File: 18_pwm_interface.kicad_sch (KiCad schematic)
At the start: 49 parts

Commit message: update -- i don't remeber what
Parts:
- R1, R10, R11, R12, R13, R14, R15, R16, R17, R18, R19, R2, R20, R21, R3, R4, R5, R6, R7, R8, R9: footprint (none) -> Resistor_SMD:R_0805_2012Metric
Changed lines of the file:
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@@
 			)
 		)
-		(property "Footprint" ""
+		(property "Footprint" "Resistor_SMD:R_0805_2012Metric"
 			(at 80.772 97.79 90)
 			(effects
@@
 			)
 		)
-		(property "Footprint" ""
+		(property "Footprint" "Resistor_SMD:R_0805_2012Metric"
 			(at 43.942 48.26 90)
 			(effects
@@
 			)
 		)
-		(property "Footprint" ""
+		(property "Footprint" "Resistor_SMD:R_0805_2012Metric"
 			(at 219.202 97.79 90)
 			(effects
@@
 			)
 		)
-		(property "Footprint" ""
+		(property "Footprint" "Resistor_SMD:R_0805_2012Metric"
 			(at 234.442 49.53 90)
 			(effects
@@
 			)
 		)
-		(property "Footprint" ""
+		(property "Footprint" "Resistor_SMD:R_0805_2012Metric"
 			(at 200.152 48.26 90)
 			(effects
@@
 			)
 		)
-		(property "Footprint" ""
+		(property "Footprint" "Resistor_SMD:R_0805_2012Metric"
 			(at 94.742 48.26 90)
 			(effects
@@
 			)
 		)
-		(property "Footprint" ""
+		(property "Footprint" "Resistor_SMD:R_0805_2012Metric"
 			(at 163.322 48.26 90)
 			(effects
@@
 			)
 		)
-		(property "Footprint" ""
+		(property "Footprint" "Resistor_SMD:R_0805_2012Metric"
 			(at 148.082 48.26 90)
 			(effects
@@
 			)
 		)
-		(property "Footprint" ""
+		(property "Footprint" "Resistor_SMD:R_0805_2012Metric"
 			(at 60.452 48.26 90)
 			(effects
@@
 			)
 		)
-		(property "Footprint" ""
+		(property "Footprint" "Resistor_SMD:R_0805_2012Metric"
 			(at 98.552 97.79 90)
 			(effects
@@
 			)
 		)
-		(property "Footprint" ""
+		(property "Footprint" "Resistor_SMD:R_0805_2012Metric"
 			(at 116.332 97.79 90)
 			(effects
@@
 			)
 		)
-		(property "Footprint" ""
+		(property "Footprint" "Resistor_SMD:R_0805_2012Metric"
 			(at 130.302 48.26 90)
 			(effects
@@
 			)
 		)
-		(property "Footprint" ""
+		(property "Footprint" "Resistor_SMD:R_0805_2012Metric"
 			(at 112.522 48.26 90)
 			(effects
@@
 			)
 		)
-		(property "Footprint" ""
+		(property "Footprint" "Resistor_SMD:R_0805_2012Metric"
 			(at 183.642 97.79 90)
 			(effects
@@
 			)
 		)
-		(property "Footprint" ""
+		(property "Footprint" "Resistor_SMD:R_0805_2012Metric"
 			(at 134.112 97.79 90)
 			(effects
@@
 			)
 		)
-		(property "Footprint" ""
+		(property "Footprint" "Resistor_SMD:R_0805_2012Metric"
 			(at 64.262 97.79 90)
 			(effects
@@
 			)
 		)
-		(property "Footprint" ""
+		(property "Footprint" "Resistor_SMD:R_0805_2012Metric"
 			(at 217.932 49.53 90)
 			(effects
@@
 			)
 		)
-		(property "Footprint" ""
+		(property "Footprint" "Resistor_SMD:R_0805_2012Metric"
 			(at 181.102 48.26 90)
 			(effects
@@
 			)
 		)
-		(property "Footprint" ""
+		(property "Footprint" "Resistor_SMD:R_0805_2012Metric"
 			(at 47.752 97.79 90)
 			(effects
@@
 			)
 		)
-		(property "Footprint" ""
+		(property "Footprint" "Resistor_SMD:R_0805_2012Metric"
 			(at 201.422 97.79 90)
 			(effects
@@
 			)
 		)
-		(property "Footprint" ""
+		(property "Footprint" "Resistor_SMD:R_0805_2012Metric"
 			(at 76.962 48.26 90)
 			(effects

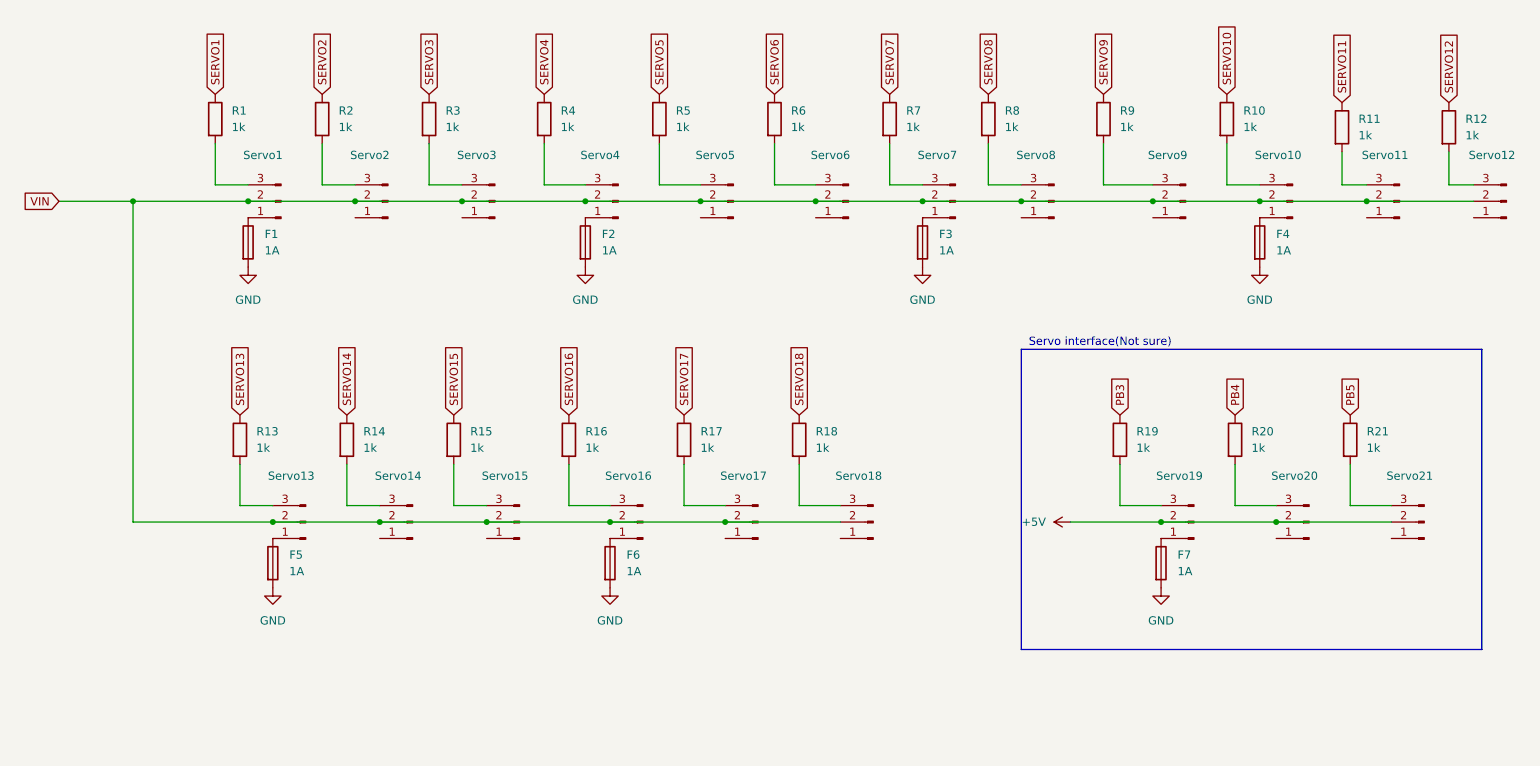
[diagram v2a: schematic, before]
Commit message: Removed redundent components
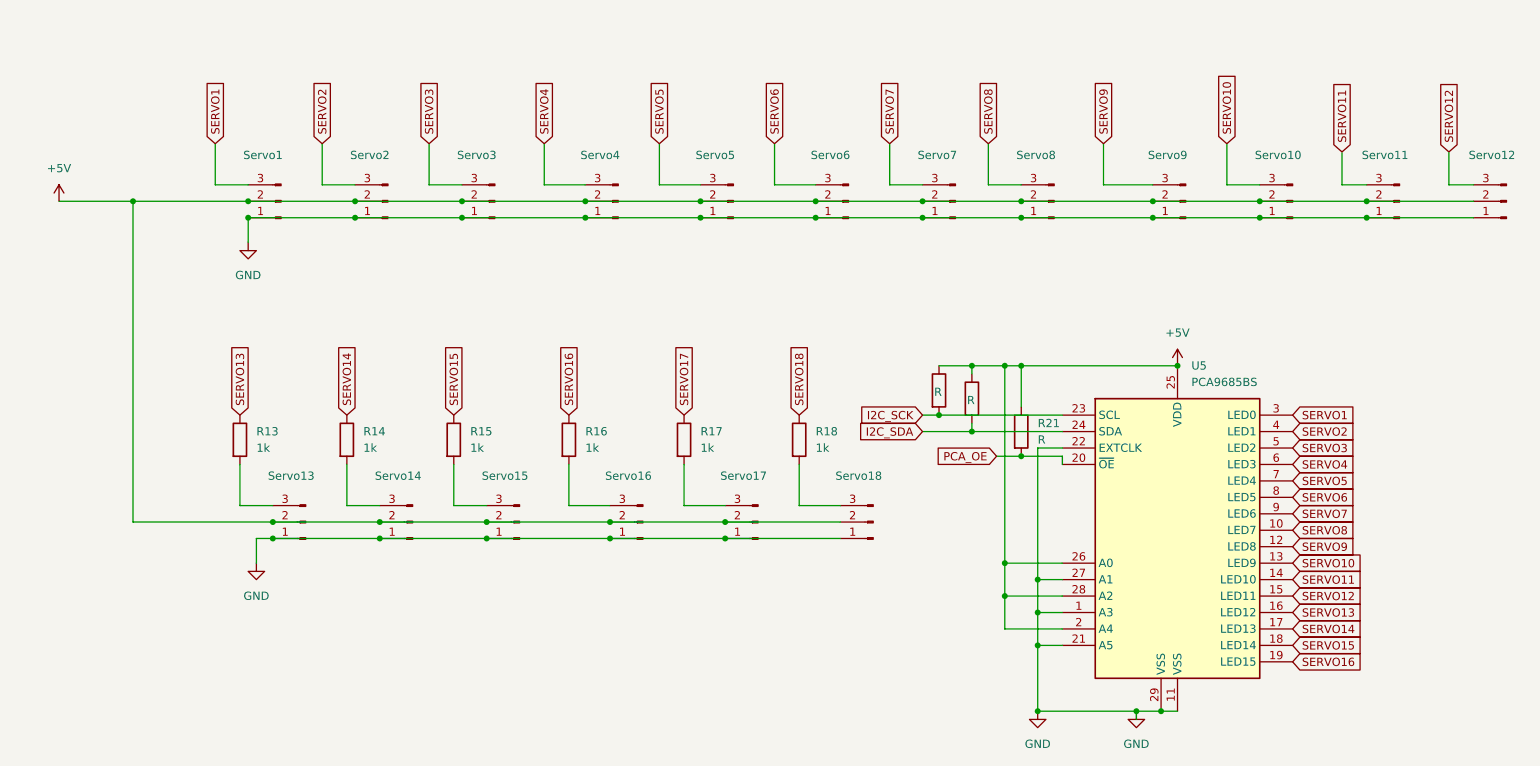
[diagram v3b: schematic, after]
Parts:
- removed F1, F2, F3, F4, F5, F6, F7: 1A, symbol Device:Fuse
- removed R1, R10, R11, R12, R2, R3, R4, R5, R6, R7, R8, R9: 1k, Resistor_SMD:R_0805_2012Metric, symbol Device:R
- removed Servo19, Servo20, Servo21: Conn_01x03_Pin, symbol Connector:Conn_01x03_Pin
- added U5: PCA9685BS, Package_DFN_QFN:QFN-28-1EP_6x6mm_P0.65mm_EP4.25x4.25mm, symbol Driver_LED:PCA9685BS
- R19, R20, R21: value 1k -> R
- Servo1, Servo10, Servo11, Servo12, Servo13, Servo14, Servo15, Servo16, Servo17, Servo18, Servo2, Servo3, Servo4, Servo5, Servo6, Servo7, Servo8, Servo9: footprint (none) -> Connector_JST:JST_XH_B3B-XH-AM_1x03_P2.50mm_Vertical
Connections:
- net PB3 is gone; now on net +5V: R19.1
- net PB4 is gone; now on net +5V: R20.1
- net PB5 is gone; now on net +5V: R21.1
- net VIN is gone; now on net +5V: Servo1.2 (Pin_2), Servo10.2 (Pin_2), Servo11.2 (Pin_2), Servo12.2 (Pin_2), Servo13.2 (Pin_2), Servo14.2 (Pin_2), Servo15.2 (Pin_2), Servo16.2 (Pin_2), Servo17.2 (Pin_2), Servo18.2 (Pin_2), Servo2.2 (Pin_2), Servo3.2 (Pin_2), Servo4.2 (Pin_2), Servo5.2 (Pin_2), Servo6.2 (Pin_2), Servo7.2 (Pin_2), Servo8.2 (Pin_2), Servo9.2 (Pin_2)
- net +5V: now also U5.2 (A4), U5.25 (VDD), U5.26 (A0), U5.28 (A2)
- net GND: now also Servo1.1 (Pin_1), Servo10.1 (Pin_1), Servo11.1 (Pin_1), Servo12.1 (Pin_1), Servo13.1 (Pin_1), Servo14.1 (Pin_1), Servo15.1 (Pin_1), Servo16.1 (Pin_1), Servo17.1 (Pin_1), Servo18.1 (Pin_1), Servo2.1 (Pin_1), Servo3.1 (Pin_1), Servo4.1 (Pin_1), Servo5.1 (Pin_1), Servo6.1 (Pin_1), Servo7.1 (Pin_1), Servo8.1 (Pin_1), Servo9.1 (Pin_1), U5.1 (A3), U5.11 (VSS), U5.21 (A5), U5.22 (EXTCLK), U5.27 (A1), U5.29 (VSS)
- net SERVO1: now also Servo1.3 (Pin_3), U5.3 (LED0)
- net SERVO10: now also Servo10.3 (Pin_3), U5.13 (LED9)
- net SERVO11: now also Servo11.3 (Pin_3), U5.14 (LED10)
- net SERVO12: now also Servo12.3 (Pin_3), U5.15 (LED11)
- net SERVO13: now also U5.16 (LED12)
- net SERVO14: now also U5.17 (LED13)
- net SERVO15: now also U5.18 (LED14)
- net SERVO16: now also U5.19 (LED15)
- net SERVO2: now also Servo2.3 (Pin_3), U5.4 (LED1)
- net SERVO3: now also Servo3.3 (Pin_3), U5.5 (LED2)
- net SERVO4: now also Servo4.3 (Pin_3), U5.6 (LED3)
- net SERVO5: now also Servo5.3 (Pin_3), U5.7 (LED4)
- net SERVO6: now also Servo6.3 (Pin_3), U5.8 (LED5)
- net SERVO7: now also Servo7.3 (Pin_3), U5.9 (LED6)
- net SERVO8: now also Servo8.3 (Pin_3), U5.10 (LED7)
- net SERVO9: now also Servo9.3 (Pin_3), U5.12 (LED8)
- net PCA_OE: now reaches R21.2
- net PCA_OE: now also U5.20 (~{OE})
- net I2C_SCK: now reaches R19.2
- net I2C_SCK: now also U5.23 (SCL)
- net I2C_SDA: now reaches R20.2
- net I2C_SDA: now also U5.24 (SDA)
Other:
- note removed: "Servo interface(Not sure)"
